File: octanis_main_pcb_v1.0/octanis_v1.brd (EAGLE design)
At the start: 82 x 50 mm, 117 parts, among them IC1 BNO055A, IC2 BME280, Q1 32.768kHz, Q2 32.768kHz, U1 TPS61201, U10 INA210, U100 RN2483, U11 DRV8836DSSR, U12 DRV8836DSSR, U2 MSP432, U3 MAX6001SOT-23, U4 DRV8836DSSR, U5 DRV8836DSSR, U6 SST25VF064C, U7 INA210, U8 INA210, U9 INA210

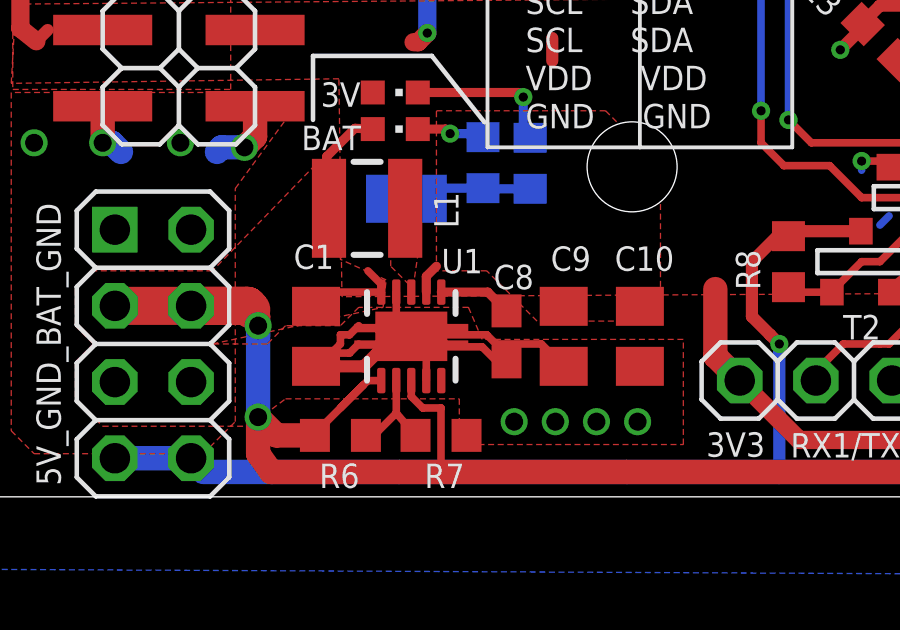
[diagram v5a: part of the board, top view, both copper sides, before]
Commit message: corrected the feedback pin error on battery DC-DC converter.
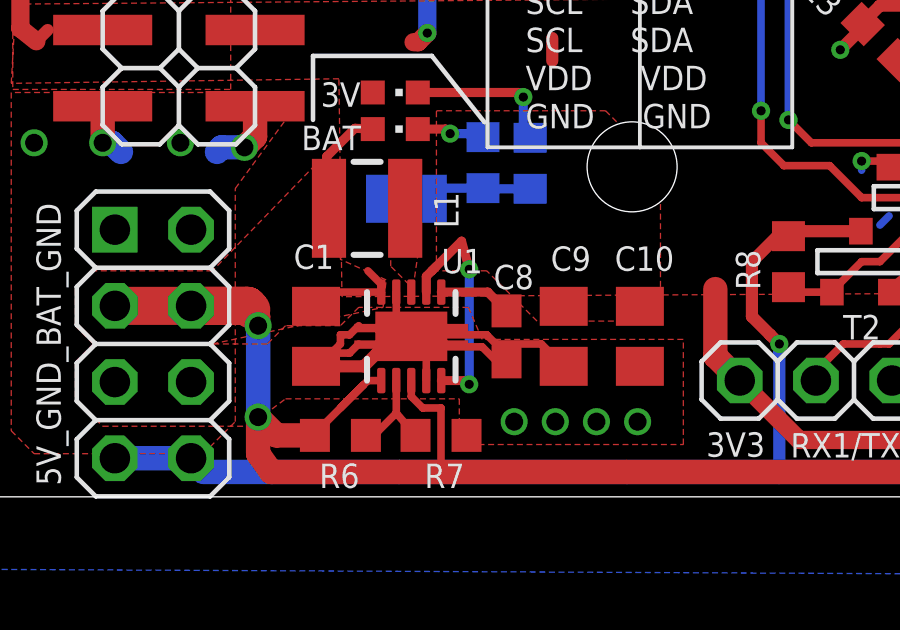
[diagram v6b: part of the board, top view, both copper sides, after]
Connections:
- net +3V3: now also U1.10
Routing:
- net +3V3: track 284.1 -> 291.3 mm, vias 10 -> 12
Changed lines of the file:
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@@
 <setting verticaltext="up"/>
 </settings>
-<grid distance="25" unitdist="mil" unit="mil" style="lines" multiple="1" display="yes" altdistance="0.025" altunitdist="inch" altunit="inch"/>
+<grid distance="12" unitdist="mil" unit="mil" style="lines" multiple="1" display="yes" altdistance="0.025" altunitdist="inch" altunit="inch"/>
 <layers>
-<layer number="1" name="Top" color="4" fill="1" visible="no" active="yes"/>
+<layer number="1" name="Top" color="4" fill="1" visible="yes" active="yes"/>
 <layer number="16" name="Bottom" color="1" fill="1" visible="yes" active="yes"/>
-<layer number="17" name="Pads" color="2" fill="1" visible="no" active="yes"/>
-<layer number="18" name="Vias" color="2" fill="1" visible="no" active="yes"/>
-<layer number="19" name="Unrouted" color="6" fill="1" visible="no" active="yes"/>
-<layer number="20" name="Dimension" color="15" fill="1" visible="no" active="yes"/>
-<layer number="21" name="tPlace" color="7" fill="1" visible="no" active="yes"/>
+<layer number="17" name="Pads" color="2" fill="1" visible="yes" active="yes"/>
+<layer number="18" name="Vias" color="2" fill="1" visible="yes" active="yes"/>
+<layer number="19" name="Unrouted" color="6" fill="1" visible="yes" active="yes"/>
+<layer number="20" name="Dimension" color="15" fill="1" visible="yes" active="yes"/>
+<layer number="21" name="tPlace" color="7" fill="1" visible="yes" active="yes"/>
 <layer number="22" name="bPlace" color="7" fill="1" visible="yes" active="yes"/>
-<layer number="23" name="tOrigins" color="15" fill="1" visible="no" active="yes"/>
+<layer number="23" name="tOrigins" color="15" fill="1" visible="yes" active="yes"/>
 <layer number="24" name="bOrigins" color="15" fill="1" visible="yes" active="yes"/>
-<layer number="25" name="tNames" color="7" fill="1" visible="no" active="yes"/>
+<layer number="25" name="tNames" color="7" fill="1" visible="yes" active="yes"/>
 <layer number="26" name="bNames" color="7" fill="1" visible="yes" active="yes"/>
-<layer number="27" name="tValues" color="7" fill="1" visible="no" active="yes"/>
-<layer number="28" name="bValues" color="7" fill="1" visible="no" active="yes"/>
+<layer number="27" name="tValues" color="7" fill="1" visible="yes" active="yes"/>
+<layer number="28" name="bValues" color="7" fill="1" visible="yes" active="yes"/>
 <layer number="29" name="tStop" color="7" fill="3" visible="no" active="yes"/>
 <layer number="30" name="bStop" color="7" fill="6" visible="no" active="yes"/>
@@
 <layer number="155" name="FabDoc3" color="7" fill="15" visible="no" active="no"/>
 <layer number="199" name="Contour" color="7" fill="1" visible="no" active="yes"/>
-<layer number="200" name="200bmp" color="15" fill="1" visible="yes" active="yes"/>
+<layer number="200" name="200bmp" color="15" fill="1" visible="no" active="yes"/>
 <layer number="201" name="201bmp" color="7" fill="1" visible="no" active="yes"/>
 <layer number="202" name="202bmp" color="7" fill="1" visible="no" active="yes"/>
@@
 <contactref element="U1" pad="2"/>
 <wire x1="14.1398" y1="7.825" x2="14.1398" y2="8.3486" width="0.3048" layer="1"/>
-<wire x1="14.1398" y1="8.3486" x2="14.478" y2="8.6868" width="0.3048" layer="1"/>
+<wire x1="14.1398" y1="8.3486" x2="14.3256" y2="8.5344" width="0.3048" layer="1"/>
 <polygon width="0.254" layer="1">
 <vertex x="14.478" y="8.5344"/>
@@
 <contactref element="JP4" pad="9"/>
 <contactref element="JP4" pad="10"/>
+<wire x1="14.3256" y1="8.5344" x2="14.478" y2="8.6868" width="0.3048" layer="1"/>
 <wire x1="24.5872" y1="4.8768" x2="23.7744" y2="5.6896" width="0.8128" layer="1"/>
 <wire x1="23.7744" y1="5.6896" x2="23.7744" y2="7.9248" width="0.8128" layer="1"/>
@@
 <wire x1="8.8171" y1="36.6068" x2="8.7863" y2="36.576" width="0.254" layer="1"/>
 <wire x1="8.7863" y1="36.576" x2="7.1628" y2="36.576" width="0.254" layer="1"/>
+<contactref element="U1" pad="10"/>
+<wire x1="14.6398" y1="4.875" x2="15.445" y2="4.875" width="0.3" layer="1"/>
+<wire x1="15.445" y1="4.875" x2="15.5702" y2="4.7498" width="0.3" layer="1"/>
+<via x="15.5702" y="4.7498" extent="1-16" drill="0.3"/>
+<wire x1="15.5702" y1="4.7498" x2="15.5702" y2="8.5852" width="0.3" layer="16"/>
+<via x="15.5702" y="8.5852" extent="1-16" drill="0.3"/>
+<wire x1="15.5702" y1="8.5852" x2="15.3162" y2="9.525" width="0.3" layer="1"/>
+<wire x1="15.3162" y1="9.525" x2="14.3256" y2="8.5344" width="0.3" layer="1"/>
 </signal>
 <signal name="M1IN2">
